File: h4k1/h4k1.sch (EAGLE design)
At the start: 191 parts, among them IC1 STM32F10XCXT6, J2 PJ-313D-AUDIO-JACK, J3 USB-AF10, K1 CHERRY-MX-LED, K10 CHERRY-MX, K11 CHERRY-MX, K12 CHERRY-MX, K13 CHERRY-MX, K14 CHERRY-MX, K15 CHERRY-MX, K16 CHERRY-MX, K17 CHERRY-MX-LED, K18 CHERRY-MX, K19 CHERRY-MX, K2 CHERRY-MX-LED, K20 CHERRY-MX, K21 CHERRY-MX, K22 CHERRY-MX, K23 CHERRY-MX, K24 CHERRY-MX, K25 CHERRY-MX-LED, K26 CHERRY-MX, K27 CHERRY-MX, K28 CHERRY-MX, K29 CHERRY-MX, K3 CHERRY-MX-LED, K30 CHERRY-MX, K31 CHERRY-MX, K32 CHERRY-MX, K33 CHERRY-MX-LED, K34 CHERRY-MX, K35 CHERRY-MX, K36 CHERRY-MX-LED, K37 CHERRY-MX-LED, K38 CHERRY-MX, K39 CHERRY-MX, K4 CHERRY-MX-LED, K40 CHERRY-MX-LED, K41 CHERRY-MX, K42 CHERRY-MX, K43 CHERRY-MX, K44 CHERRY-MX, K45 CHERRY-MX, K46 CHERRY-MX-LED, K5 CHERRY-MX-LED, K6 CHERRY-MX-LED, K65 EVQPUL02K, K66 EVQPUL02K, K67 K3-1280S-F2, K7 CHERRY-MX-LED, K8 CHERRY-MX-LED, K9 CHERRY-MX-LED, T1 DBG, U1 G850G, U3 PCM2704CDB, X4 12M

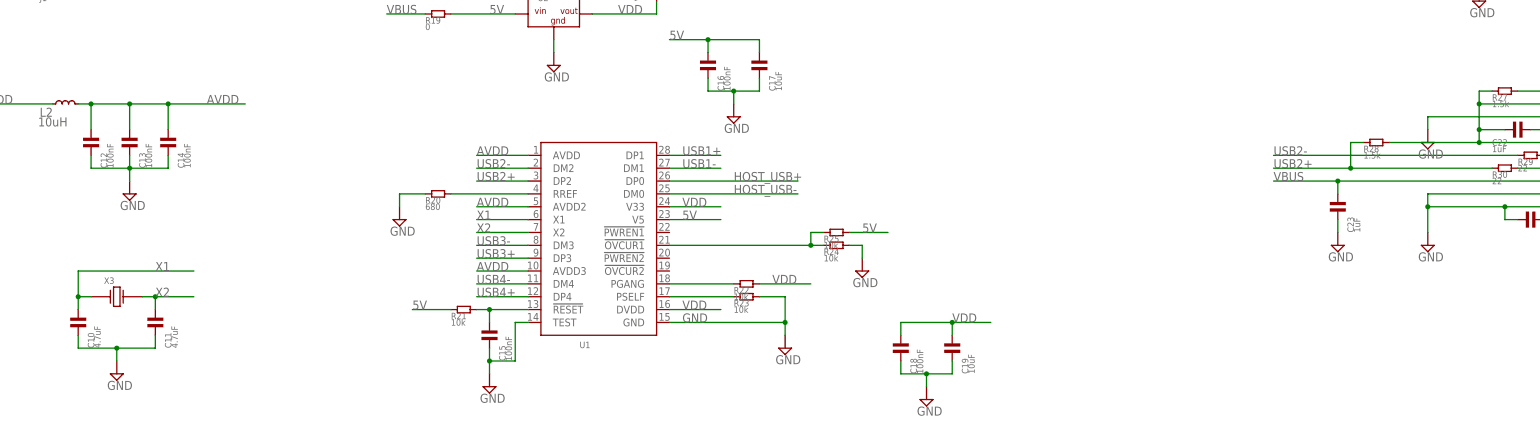
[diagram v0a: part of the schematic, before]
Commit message: resolve drc problem
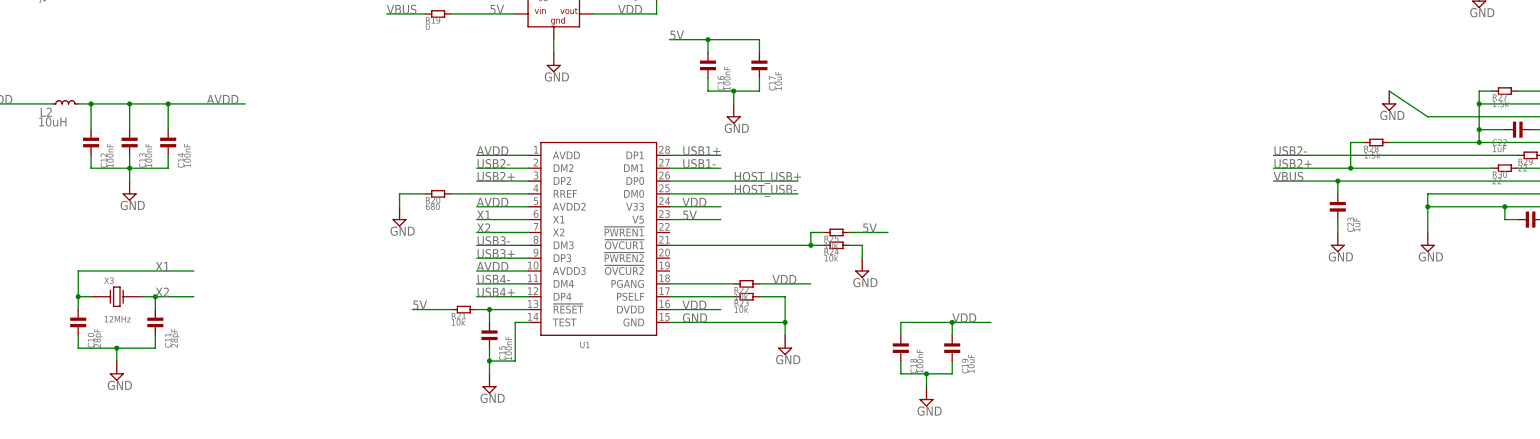
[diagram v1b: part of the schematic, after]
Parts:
- C10, C11: value 4.7uF -> 28pF
- X3: value (none) -> 12MHz
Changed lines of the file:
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@@
 <part name="SUPPLY6" library="supply2" deviceset="GND" device=""/>
 <part name="U1" library="hqc-communication" deviceset="G850G" device=""/>
-<part name="X3" library="hqc-crystal" deviceset="49S-CRYSTAL" device=""/>
-<part name="C10" library="hqc" deviceset="C-0805" device="" value="4.7uF"/>
-<part name="C11" library="hqc" deviceset="C-0805" device="" value="4.7uF"/>
+<part name="X3" library="hqc-crystal" deviceset="49S-CRYSTAL" device="" value="12MHz"/>
+<part name="C10" library="hqc" deviceset="C-0805" device="" value="28pF"/>
+<part name="C11" library="hqc" deviceset="C-0805" device="" value="28pF"/>
 <part name="SUPPLY7" library="supply2" deviceset="GND" device=""/>
 <part name="R19" library="hqc" deviceset="R-0805" device="" value="0"/>
@@
 <instance part="R27" gate="G$1" x="241.3" y="236.22"/>
 <instance part="C22" gate="G$1" x="243.84" y="228.6"/>
-<instance part="SUPPLY18" gate="GND" x="226.06" y="226.06"/>
+<instance part="SUPPLY18" gate="GND" x="218.44" y="233.68"/>
 <instance part="R28" gate="G$1" x="215.9" y="226.06"/>
 <instance part="R29" gate="G$1" x="246.38" y="223.52"/>
@@
 <junction x="248.92" y="228.6"/>
 <wire x1="248.92" y1="231.14" x2="226.06" y2="231.14" width="0.1524" layer="91"/>
-<wire x1="226.06" y1="231.14" x2="226.06" y2="228.6" width="0.1524" layer="91"/>
+<wire x1="226.06" y1="231.14" x2="218.44" y2="236.22" width="0.1524" layer="91"/>
 <pinref part="SUPPLY18" gate="GND" pin="GND"/>
 </segment>

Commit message: layout done
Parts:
- C20, C21: value (none) -> 28pF
- U1: value G850G -> GL850G; device hqc-communication:G850G -> hqc-communication:GL850G
- X4: value 12M -> 12MHz
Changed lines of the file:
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@@
 <part name="X2" library="hqc-crystal" deviceset="CSTCC8M00G53-R0-7230-8M-15P-RESONATOR" device=""/>
 <part name="SUPPLY6" library="supply2" deviceset="GND" device=""/>
-<part name="U1" library="hqc-communication" deviceset="G850G" device=""/>
+<part name="U1" library="hqc-communication" deviceset="GL850G" device=""/>
 <part name="X3" library="hqc-crystal" deviceset="49S-CRYSTAL" device="" value="12MHz"/>
 <part name="C10" library="hqc" deviceset="C-0805" device="" value="28pF"/>
@@
 <part name="U3" library="hqc" deviceset="PCM2704CDB" device=""/>
 <part name="R26" library="hqc" deviceset="R-0805" device="" value="1M"/>
-<part name="X4" library="hqc-crystal" deviceset="49S-CRYSTAL" device="" value="12M"/>
-<part name="C20" library="hqc" deviceset="C-0805" device=""/>
-<part name="C21" library="hqc" deviceset="C-0805" device=""/>
+<part name="X4" library="hqc-crystal" deviceset="49S-CRYSTAL" device="" value="12MHz"/>
+<part name="C20" library="hqc" deviceset="C-0805" device="" value="28pF"/>
+<part name="C21" library="hqc" deviceset="C-0805" device="" value="28pF"/>
 <part name="SUPPLY16" library="supply2" deviceset="GND" device=""/>
 <part name="SUPPLY17" library="supply2" deviceset="GND" device=""/>
@@
 <instance part="X2" gate="CSTCC8M00G53-R0" x="231.14" y="35.56"/>
 <instance part="SUPPLY6" gate="GND" x="231.14" y="22.86"/>
-<instance part="U1" gate="GL750G" x="63.5" y="208.28"/>
+<instance part="U1" gate="GL850G" x="63.5" y="208.28"/>
 <instance part="X3" gate="G$1" x="-33.02" y="195.58"/>
 <instance part="C10" gate="G$1" x="-40.64" y="190.5" rot="R90"/>
@@
 </segment>
 <segment>
-<pinref part="U1" gate="GL750G" pin="V33"/>
+<pinref part="U1" gate="GL850G" pin="V33"/>
 <wire x1="76.2" y1="213.36" x2="86.36" y2="213.36" width="0.1524" layer="91"/>
 <label x="78.74" y="213.36" size="1.778" layer="95"/>
@@
 </segment>
 <segment>
-<pinref part="U1" gate="GL750G" pin="DVDD"/>
+<pinref part="U1" gate="GL850G" pin="DVDD"/>
 <wire x1="76.2" y1="193.04" x2="86.36" y2="193.04" width="0.1524" layer="91"/>
 <label x="78.74" y="193.04" size="1.778" layer="95"/>
@@
 </segment>
 <segment>
-<pinref part="U1" gate="GL750G" pin="TEST"/>
+<pinref part="U1" gate="GL850G" pin="TEST"/>
 <wire x1="48.26" y1="190.5" x2="45.72" y2="190.5" width="0.1524" layer="91"/>
 <wire x1="45.72" y1="190.5" x2="45.72" y2="182.88" width="0.1524" layer="91"/>
@@
 </segment>
 <segment>
-<pinref part="U1" gate="GL750G" pin="GND"/>
+<pinref part="U1" gate="GL850G" pin="GND"/>
 <wire x1="76.2" y1="190.5" x2="99.06" y2="190.5" width="0.1524" layer="91"/>
 <label x="78.74" y="190.5" size="1.778" layer="95"/>
@@
 <net name="X1" class="0">
 <segment>
-<pinref part="U1" gate="GL750G" pin="X1"/>
+<pinref part="U1" gate="GL850G" pin="X1"/>
 <wire x1="48.26" y1="210.82" x2="38.1" y2="210.82" width="0.1524" layer="91"/>
 <label x="38.1" y="210.82" size="1.778" layer="95"/>
@@
 <net name="X2" class="0">
 <segment>
-<pinref part="U1" gate="GL750G" pin="X2"/>
+<pinref part="U1" gate="GL850G" pin="X2"/>
 <wire x1="48.26" y1="208.28" x2="38.1" y2="208.28" width="0.1524" layer="91"/>
 <label x="38.1" y="208.28" size="1.778" layer="95"/>
@@
 </segment>
 <segment>
-<pinref part="U1" gate="GL750G" pin="V5"/>
+<pinref part="U1" gate="GL850G" pin="V5"/>
 <wire x1="76.2" y1="210.82" x2="86.36" y2="210.82" width="0.1524" layer="91"/>
 <label x="78.74" y="210.82" size="1.778" layer="95"/>
@@
 <net name="USB2-" class="0">
 <segment>
-<pinref part="U1" gate="GL750G" pin="DM2"/>
+<pinref part="U1" gate="GL850G" pin="DM2"/>
 <wire x1="48.26" y1="220.98" x2="38.1" y2="220.98" width="0.1524" layer="91"/>
 <label x="38.1" y="220.98" size="1.778" layer="95"/>
@@
 <net name="USB2+" class="0">
 <segment>
-<pinref part="U1" gate="GL750G" pin="DP2"/>
+<pinref part="U1" gate="GL850G" pin="DP2"/>
 <wire x1="38.1" y1="218.44" x2="48.26" y2="218.44" width="0.1524" layer="91"/>
 <label x="38.1" y="218.44" size="1.778" layer="95"/>
@@
 <net name="AVDD" class="0">
 <segment>
-<pinref part="U1" gate="GL750G" pin="AVDD"/>
+<pinref part="U1" gate="GL850G" pin="AVDD"/>
 <wire x1="48.26" y1="223.52" x2="38.1" y2="223.52" width="0.1524" layer="91"/>
 <label x="38.1" y="223.52" size="1.778" layer="95"/>
 </segment>
 <segment>
-<pinref part="U1" gate="GL750G" pin="AVDD2"/>
+<pinref part="U1" gate="GL850G" pin="AVDD2"/>
 <wire x1="48.26" y1="213.36" x2="38.1" y2="213.36" width="0.1524" layer="91"/>
 <label x="38.1" y="213.36" size="1.778" layer="95"/>
 </segment>
 <segment>
-<pinref part="U1" gate="GL750G" pin="AVDD3"/>
+<pinref part="U1" gate="GL850G" pin="AVDD3"/>
 <wire x1="48.26" y1="200.66" x2="38.1" y2="200.66" width="0.1524" layer="91"/>
 <label x="38.1" y="200.66" size="1.778" layer="95"/>
@@
 <net name="N$26" class="0">
 <segment>
-<pinref part="U1" gate="GL750G" pin="RREF"/>
+<pinref part="U1" gate="GL850G" pin="RREF"/>
 <pinref part="R20" gate="G$1" pin="P$2"/>
 <wire x1="48.26" y1="215.9" x2="33.02" y2="215.9" width="0.1524" layer="91"/>
@@
 <net name="USB3-" class="0">
 <segment>
-<pinref part="U1" gate="GL750G" pin="DM3"/>
+<pinref part="U1" gate="GL850G" pin="DM3"/>
 <wire x1="48.26" y1="205.74" x2="38.1" y2="205.74" width="0.1524" layer="91"/>
 <label x="38.1" y="205.74" size="1.778" layer="95"/>
@@
 <net name="USB3+" class="0">
 <segment>
-<pinref part="U1" gate="GL750G" pin="DP3"/>
+<pinref part="U1" gate="GL850G" pin="DP3"/>
 <wire x1="38.1" y1="203.2" x2="48.26" y2="203.2" width="0.1524" layer="91"/>
 <label x="38.1" y="203.2" size="1.778" layer="95"/>
@@
 <net name="USB4-" class="0">
 <segment>
-<pinref part="U1" gate="GL750G" pin="DM4"/>
+<pinref part="U1" gate="GL850G" pin="DM4"/>
 <wire x1="48.26" y1="198.12" x2="38.1" y2="198.12" width="0.1524" layer="91"/>
 <label x="38.1" y="198.12" size="1.778" layer="95"/>
@@
 <net name="USB4+" class="0">
 <segment>
-<pinref part="U1" gate="GL750G" pin="DP4"/>
+<pinref part="U1" gate="GL850G" pin="DP4"/>
 <wire x1="38.1" y1="195.58" x2="48.26" y2="195.58" width="0.1524" layer="91"/>
 <label x="38.1" y="195.58" size="1.778" layer="95"/>
@@
 <net name="N$24" class="0">
 <segment>
-<pinref part="U1" gate="GL750G" pin="!RESET"/>
+<pinref part="U1" gate="GL850G" pin="!RESET"/>
 <pinref part="R21" gate="G$1" pin="P$2"/>
 <wire x1="48.26" y1="193.04" x2="40.64" y2="193.04" width="0.1524" layer="91"/>
@@
 <net name="USB1+" class="0">
 <segment>
-<pinref part="U1" gate="GL750G" pin="DP1"/>
+<pinref part="U1" gate="GL850G" pin="DP1"/>
 <wire x1="76.2" y1="223.52" x2="86.36" y2="223.52" width="0.1524" layer="91"/>
 <label x="78.74" y="223.52" size="1.778" layer="95"/>
@@
 <net name="USB1-" class="0">
 <segment>
-<pinref part="U1" gate="GL750G" pin="DM1"/>
+<pinref part="U1" gate="GL850G" pin="DM1"/>
 <wire x1="76.2" y1="220.98" x2="86.36" y2="220.98" width="0.1524" layer="91"/>
 <label x="78.74" y="220.98" size="1.778" layer="95"/>
@@
 <net name="HOST_USB+" class="0">
 <segment>
-<pinref part="U1" gate="GL750G" pin="DP0"/>
+<pinref part="U1" gate="GL850G" pin="DP0"/>
 <wire x1="76.2" y1="218.44" x2="101.6" y2="218.44" width="0.1524" layer="91"/>
 <label x="88.9" y="218.44" size="1.778" layer="95"/>
@@
 <net name="HOST_USB-" class="0">
 <segment>
-<pinref part="U1" gate="GL750G" pin="DM0"/>
+<pinref part="U1" gate="GL850G" pin="DM0"/>
 <wire x1="76.2" y1="215.9" x2="101.6" y2="215.9" width="0.1524" layer="91"/>
 <label x="88.9" y="215.9" size="1.778" layer="95"/>
@@
 <net name="N$28" class="0">
 <segment>
-<pinref part="U1" gate="GL750G" pin="PGANG"/>
+<pinref part="U1" gate="GL850G" pin="PGANG"/>
 <pinref part="R22" gate="G$1" pin="P$1"/>
 <wire x1="76.2" y1="198.12" x2="88.9" y2="198.12" width="0.1524" layer="91"/>
@@
 <net name="N$30" class="0">
 <segment>
-<pinref part="U1" gate="GL750G" pin="PSELF"/>
+<pinref part="U1" gate="GL850G" pin="PSELF"/>
 <pinref part="R23" gate="G$1" pin="P$1"/>
 <wire x1="76.2" y1="195.58" x2="88.9" y2="195.58" width="0.1524" layer="91"/>
@@
 <net name="N$34" class="0">
 <segment>
-<pinref part="U1" gate="GL750G" pin="!OVCUR1"/>
+<pinref part="U1" gate="GL850G" pin="!OVCUR1"/>
 <pinref part="R24" gate="G$1" pin="P$1"/>
 <wire x1="76.2" y1="205.74" x2="104.14" y2="205.74" width="0.1524" layer="91"/>

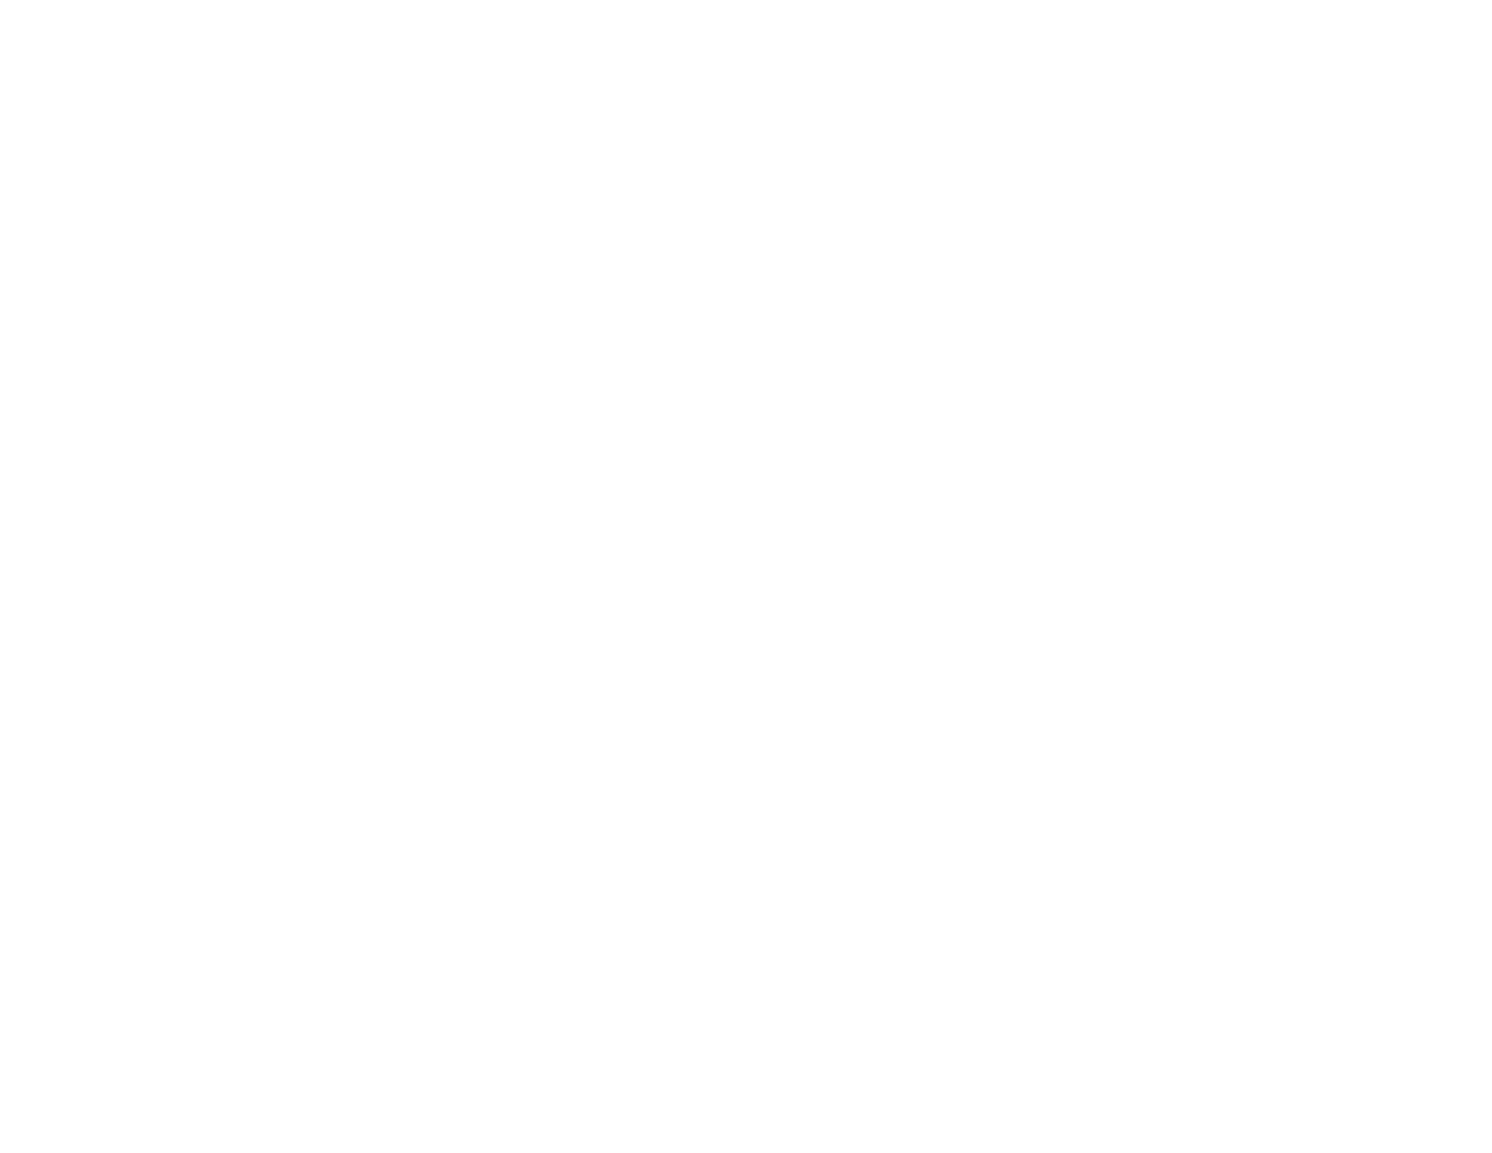
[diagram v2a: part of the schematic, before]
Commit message: add mounting holes
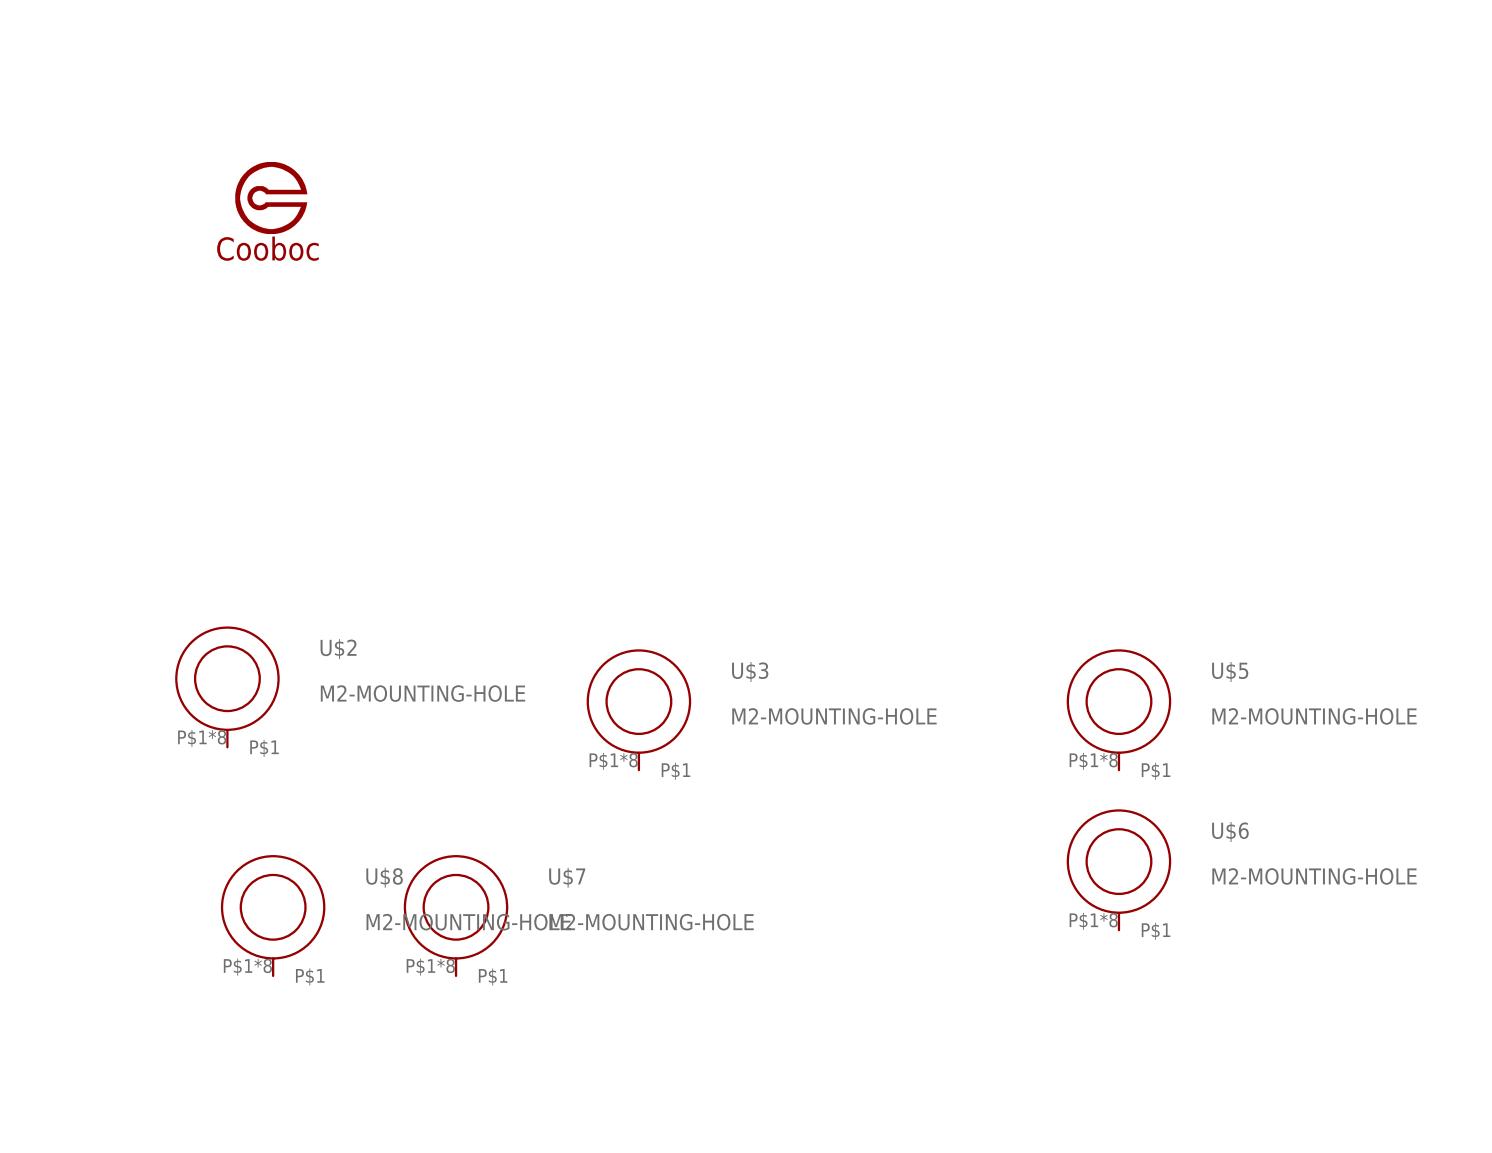
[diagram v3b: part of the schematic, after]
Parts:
- added U$1: COOBOC-PLACE, hqc-logo:COOBOC-PLACE
- added U$2, U$3, U$5, U$6, U$7, U$8: M2-MOUNTING-HOLE, hqc:M2-MOUNTING-HOLE
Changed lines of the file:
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@@
 <part name="VDD17" library="supply1" deviceset="VDD" device=""/>
 <part name="SUPPLY31" library="supply2" deviceset="GND" device=""/>
+<part name="U$1" library="hqc-logo" deviceset="COOBOC-PLACE" device=""/>
+<part name="U$2" library="hqc" deviceset="M2-MOUNTING-HOLE" device=""/>
+<part name="U$3" library="hqc" deviceset="M2-MOUNTING-HOLE" device=""/>
+<part name="U$5" library="hqc" deviceset="M2-MOUNTING-HOLE" device=""/>
+<part name="U$6" library="hqc" deviceset="M2-MOUNTING-HOLE" device=""/>
+<part name="U$7" library="hqc" deviceset="M2-MOUNTING-HOLE" device=""/>
+<part name="U$8" library="hqc" deviceset="M2-MOUNTING-HOLE" device=""/>
 </parts>
 <sheets>
@@
 <instance part="VDD17" gate="G$1" x="78.74" y="106.68"/>
 <instance part="SUPPLY31" gate="GND" x="78.74" y="88.9"/>
+<instance part="U$1" gate="G$1" x="627.38" y="-50.8"/>
+<instance part="U$2" gate="G$1" x="622.3" y="-101.6"/>
+<instance part="U$3" gate="G$1" x="668.02" y="-104.14"/>
+<instance part="U$5" gate="G$1" x="721.36" y="-104.14"/>
+<instance part="U$6" gate="G$1" x="721.36" y="-121.92"/>
+<instance part="U$7" gate="G$1" x="647.7" y="-127"/>
+<instance part="U$8" gate="G$1" x="627.38" y="-127"/>
 </instances>
 <busses>
